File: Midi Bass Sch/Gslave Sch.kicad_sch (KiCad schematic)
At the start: 12 parts, among them SW6 G-slave Reset, U8 PIC16F1789

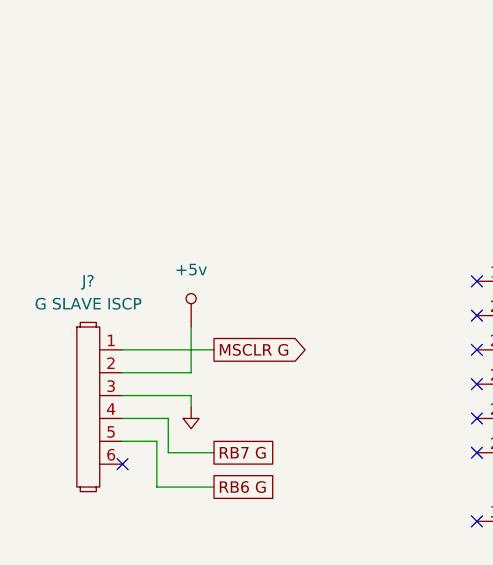
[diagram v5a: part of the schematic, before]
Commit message: started basic pcb layout for Master pic
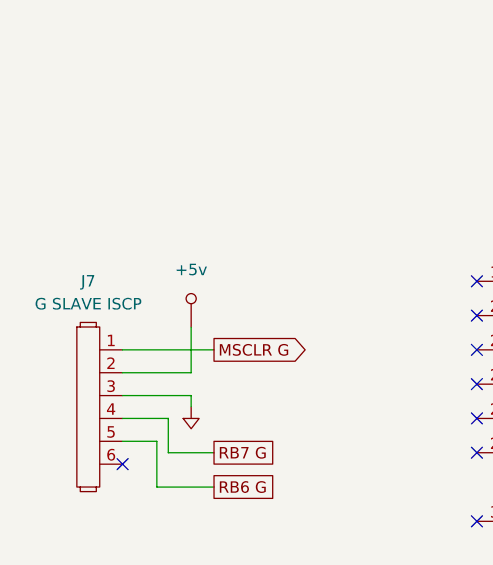
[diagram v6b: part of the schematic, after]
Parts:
- gave numbers to parts that had none: 1
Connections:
- net MSCLR G: now also D20.1; no longer D20.2
- net at C6.1, R55.1, SW6.2: now also D20.2; no longer D20.1
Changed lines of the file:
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@@
 		(dnp no)
 		(fields_autoplaced yes)
-		(property "Reference" "J?"
+		(property "Reference" "J7"
 			(at 25.4 46.99 0)
 			(effects
@@
 			(project "Midi Bass Sch"
 				(path "/06818073-fb22-48ee-acc5-6dedd827034e/a79027be-e76c-43a0-a80a-a6c6a159c340"
-					(reference "J?")
+					(reference "J7")
 					(unit 1)
 				)
@@
 		(dnp no)
 		(fields_autoplaced yes)
-		(property "Reference" "#PWR084"
+		(property "Reference" "#PWR088"
 			(at 175.26 125.73 0)
 			(effects
@@
 			(project "Midi Bass Sch"
 				(path "/06818073-fb22-48ee-acc5-6dedd827034e/a79027be-e76c-43a0-a80a-a6c6a159c340"
-					(reference "#PWR084")
+					(reference "#PWR088")
 					(unit 1)
 				)
@@
 		(dnp no)
 		(fields_autoplaced yes)
-		(property "Reference" "#PWR081"
+		(property "Reference" "#PWR085"
 			(at 46.99 138.43 0)
 			(effects
@@
 			(project "Midi Bass Sch"
 				(path "/06818073-fb22-48ee-acc5-6dedd827034e/a79027be-e76c-43a0-a80a-a6c6a159c340"
-					(reference "#PWR081")
+					(reference "#PWR085")
 					(unit 1)
 				)
@@
 		(dnp no)
 		(fields_autoplaced yes)
-		(property "Reference" "#PWR083"
+		(property "Reference" "#PWR087"
 			(at 108.8644 20.4216 0)
 			(effects
@@
 			(project "Midi Bass Sch"
 				(path "/06818073-fb22-48ee-acc5-6dedd827034e/a79027be-e76c-43a0-a80a-a6c6a159c340"
-					(reference "#PWR083")
+					(reference "#PWR087")
 					(unit 1)
 				)
@@
 		(dnp no)
 		(fields_autoplaced yes)
-		(property "Reference" "#PWR080"
+		(property "Reference" "#PWR084"
 			(at 51.7144 116.9416 0)
 			(effects
@@
 			(project "Midi Bass Sch"
 				(path "/06818073-fb22-48ee-acc5-6dedd827034e/a79027be-e76c-43a0-a80a-a6c6a159c340"
-					(reference "#PWR080")
+					(reference "#PWR084")
 					(unit 1)
 				)
@@
 		(dnp no)
 		(fields_autoplaced yes)
-		(property "Reference" "#PWR082"
+		(property "Reference" "#PWR086"
 			(at 101.6 157.48 0)
 			(effects
@@
 			(project "Midi Bass Sch"
 				(path "/06818073-fb22-48ee-acc5-6dedd827034e/a79027be-e76c-43a0-a80a-a6c6a159c340"
-					(reference "#PWR082")
+					(reference "#PWR086")
 					(unit 1)
 				)
@@
 		(dnp no)
 		(fields_autoplaced yes)
-		(property "Reference" "#PWR0326"
+		(property "Reference" "#PWR082"
 			(at 41.5544 47.0916 0)
 			(effects
@@
 			(project "Midi Bass Sch"
 				(path "/06818073-fb22-48ee-acc5-6dedd827034e/a79027be-e76c-43a0-a80a-a6c6a159c340"
-					(reference "#PWR0326")
+					(reference "#PWR082")
 					(unit 1)
 				)
@@
 		(dnp no)
 		(fields_autoplaced yes)
-		(property "Reference" "#PWR079"
+		(property "Reference" "#PWR081"
 			(at 25.4 139.7 0)
 			(effects
@@
 			(project "Midi Bass Sch"
 				(path "/06818073-fb22-48ee-acc5-6dedd827034e/a79027be-e76c-43a0-a80a-a6c6a159c340"
-					(reference "#PWR079")
+					(reference "#PWR081")
 					(unit 1)
 				)
@@
 		(dnp no)
 		(fields_autoplaced yes)
-		(property "Reference" "#PWR0327"
+		(property "Reference" "#PWR083"
 			(at 36.83 59.69 0)
 			(effects
@@
 			(project "Midi Bass Sch"
 				(path "/06818073-fb22-48ee-acc5-6dedd827034e/a79027be-e76c-43a0-a80a-a6c6a159c340"
-					(reference "#PWR0327")
+					(reference "#PWR083")
 					(unit 1)
 				)
@@
 		(dnp no)
 		(fields_autoplaced yes)
-		(property "Reference" "#PWR085"
+		(property "Reference" "#PWR089"
 			(at 189.23 123.19 0)
 			(effects
@@
 			(project "Midi Bass Sch"
 				(path "/06818073-fb22-48ee-acc5-6dedd827034e/a79027be-e76c-43a0-a80a-a6c6a159c340"
-					(reference "#PWR085")
-					(unit 1)
-				)
+					(reference "#PWR089")
+					(unit 1)
+				)

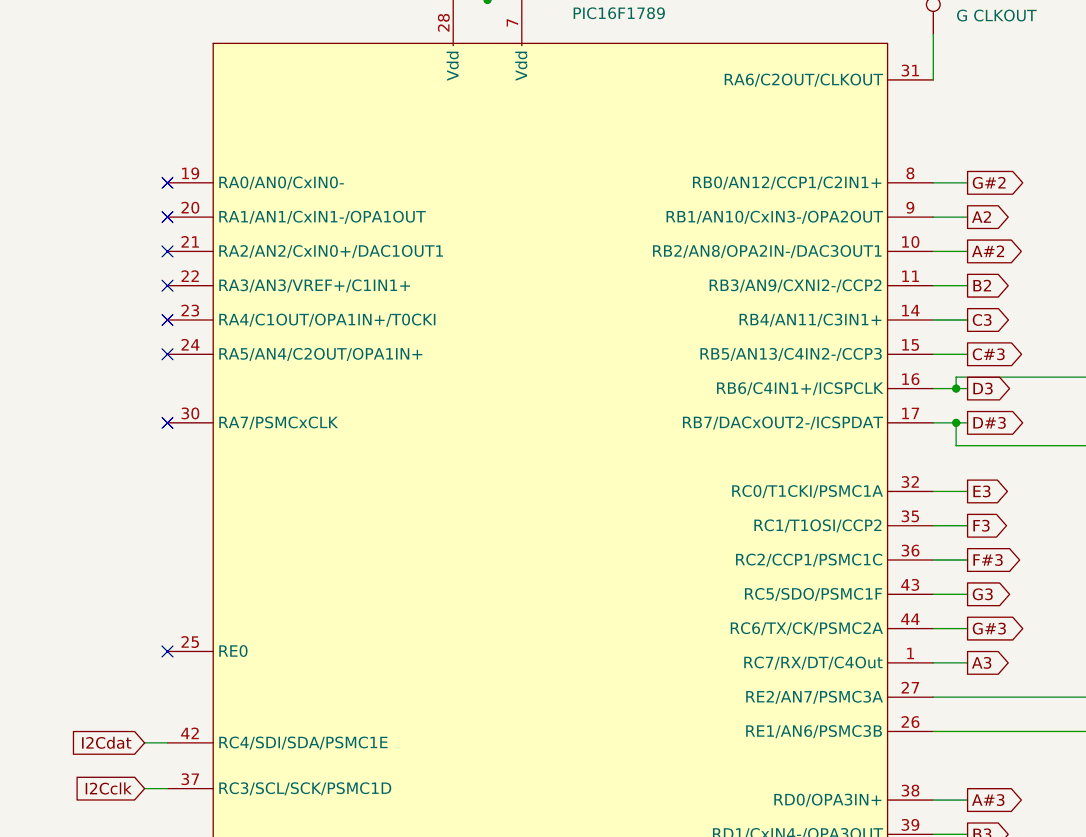
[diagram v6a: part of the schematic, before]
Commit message: updated schematic to reflect code
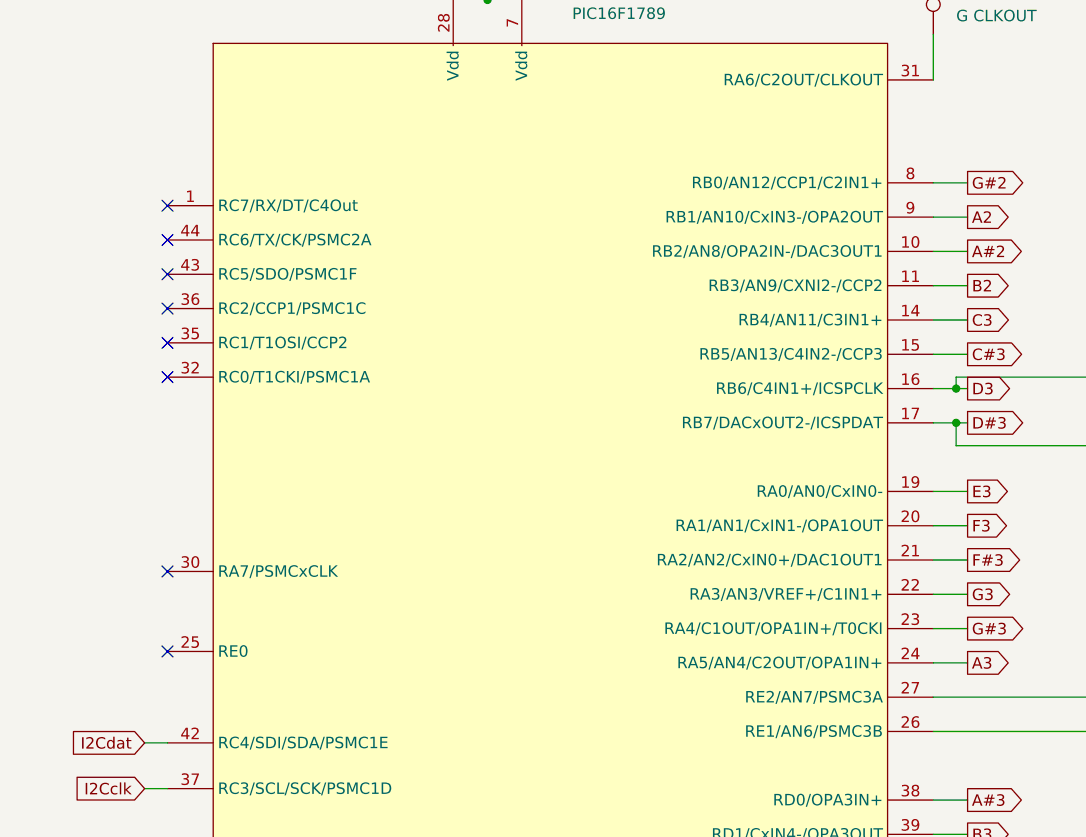
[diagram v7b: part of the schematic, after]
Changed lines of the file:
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@@
 	)
 	(no_connect
-		(at 68.58 66.04)
+		(at 68.58 68.58)
 	)
 	(no_connect
@@
 	)
 	(no_connect
-		(at 68.58 73.66)
+		(at 68.58 90.17)
 	)
 	(no_connect
-		(at 68.58 54.61)
+		(at 68.58 57.15)
 	)
 	(no_connect
@@
 	)
 	(no_connect
-		(at 68.58 62.23)
+		(at 68.58 64.77)
 	)
 	(no_connect
-		(at 68.58 46.99)
+		(at 68.58 49.53)
 	)
 	(no_connect
-		(at 68.58 58.42)
+		(at 68.58 60.96)
 	)
 	(no_connect
-		(at 68.58 50.8)
+		(at 68.58 53.34)
 	)
 	(wire

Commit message: working on troubleshooting section of report
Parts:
- renumbered J7 to J8, R54 to R66, R55 to R67, R56 to R68, R57 to R69, U8 to U10
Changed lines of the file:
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@@
 		(dnp no)
 		(fields_autoplaced yes)
-		(property "Reference" "R56"
+		(property "Reference" "R68"
 			(at 177.8 111.7599 90)
 			(effects
@@
 			(project "Midi Bass Sch"
 				(path "/06818073-fb22-48ee-acc5-6dedd827034e/a79027be-e76c-43a0-a80a-a6c6a159c340"
-					(reference "R56")
+					(reference "R68")
 					(unit 1)
 				)
@@
 		(dnp no)
 		(fields_autoplaced yes)
-		(property "Reference" "R55"
+		(property "Reference" "R67"
 			(at 49.53 124.4599 90)
 			(effects
@@
 			(project "Midi Bass Sch"
 				(path "/06818073-fb22-48ee-acc5-6dedd827034e/a79027be-e76c-43a0-a80a-a6c6a159c340"
-					(reference "R55")
+					(reference "R67")
 					(unit 1)
 				)
@@
 		(dnp no)
 		(fields_autoplaced yes)
-		(property "Reference" "J7"
+		(property "Reference" "J8"
 			(at 25.4 46.99 0)
 			(effects
@@
 			(project "Midi Bass Sch"
 				(path "/06818073-fb22-48ee-acc5-6dedd827034e/a79027be-e76c-43a0-a80a-a6c6a159c340"
-					(reference "J7")
+					(reference "J8")
 					(unit 1)
 				)
@@
 		(dnp no)
 		(fields_autoplaced yes)
-		(property "Reference" "R57"
+		(property "Reference" "R69"
 			(at 191.77 109.2199 90)
 			(effects
@@
 			(project "Midi Bass Sch"
 				(path "/06818073-fb22-48ee-acc5-6dedd827034e/a79027be-e76c-43a0-a80a-a6c6a159c340"
-					(reference "R57")
+					(reference "R69")
 					(unit 1)
 				)
@@
 		(on_board yes)
 		(dnp no)
-		(property "Reference" "U8"
+		(property "Reference" "U10"
 			(at 113.538 25.4 0)
 			(effects
@@
 			(project "Midi Bass Sch"
 				(path "/06818073-fb22-48ee-acc5-6dedd827034e/a79027be-e76c-43a0-a80a-a6c6a159c340"
-					(reference "U8")
+					(reference "U10")
 					(unit 1)
 				)
@@
 		(dnp no)
 		(fields_autoplaced yes)
-		(property "Reference" "#PWR088"
+		(property "Reference" "#PWR0102"
 			(at 175.26 125.73 0)
 			(effects
@@
 			(project "Midi Bass Sch"
 				(path "/06818073-fb22-48ee-acc5-6dedd827034e/a79027be-e76c-43a0-a80a-a6c6a159c340"
-					(reference "#PWR088")
+					(reference "#PWR0102")
 					(unit 1)
 				)
@@
 		(dnp no)
 		(fields_autoplaced yes)
-		(property "Reference" "#PWR085"
+		(property "Reference" "#PWR099"
 			(at 46.99 138.43 0)
 			(effects
@@
 			(project "Midi Bass Sch"
 				(path "/06818073-fb22-48ee-acc5-6dedd827034e/a79027be-e76c-43a0-a80a-a6c6a159c340"
-					(reference "#PWR085")
+					(reference "#PWR099")
 					(unit 1)
 				)
@@
 		(dnp no)
 		(fields_autoplaced yes)
-		(property "Reference" "#PWR087"
+		(property "Reference" "#PWR0101"
 			(at 108.8644 20.4216 0)
 			(effects
@@
 			(project "Midi Bass Sch"
 				(path "/06818073-fb22-48ee-acc5-6dedd827034e/a79027be-e76c-43a0-a80a-a6c6a159c340"
-					(reference "#PWR087")
+					(reference "#PWR0101")
 					(unit 1)
 				)
@@
 		(dnp no)
 		(fields_autoplaced yes)
-		(property "Reference" "#PWR084"
+		(property "Reference" "#PWR098"
 			(at 51.7144 116.9416 0)
 			(effects
@@
 			(project "Midi Bass Sch"
 				(path "/06818073-fb22-48ee-acc5-6dedd827034e/a79027be-e76c-43a0-a80a-a6c6a159c340"
-					(reference "#PWR084")
+					(reference "#PWR098")
 					(unit 1)
 				)
@@
 		(dnp no)
 		(fields_autoplaced yes)
-		(property "Reference" "#PWR086"
+		(property "Reference" "#PWR0100"
 			(at 101.6 157.48 0)
 			(effects
@@
 			(project "Midi Bass Sch"
 				(path "/06818073-fb22-48ee-acc5-6dedd827034e/a79027be-e76c-43a0-a80a-a6c6a159c340"
-					(reference "#PWR086")
+					(reference "#PWR0100")
 					(unit 1)
 				)
@@
 		(dnp no)
 		(fields_autoplaced yes)
-		(property "Reference" "#PWR082"
+		(property "Reference" "#PWR096"
 			(at 41.5544 47.0916 0)
 			(effects
@@
 			(project "Midi Bass Sch"
 				(path "/06818073-fb22-48ee-acc5-6dedd827034e/a79027be-e76c-43a0-a80a-a6c6a159c340"
-					(reference "#PWR082")
+					(reference "#PWR096")
 					(unit 1)
 				)
@@
 		(dnp no)
 		(fields_autoplaced yes)
-		(property "Reference" "#PWR081"
+		(property "Reference" "#PWR095"
 			(at 25.4 139.7 0)
 			(effects
@@
 			(project "Midi Bass Sch"
 				(path "/06818073-fb22-48ee-acc5-6dedd827034e/a79027be-e76c-43a0-a80a-a6c6a159c340"
-					(reference "#PWR081")
+					(reference "#PWR095")
 					(unit 1)
 				)
@@
 		(dnp no)
 		(fields_autoplaced yes)
-		(property "Reference" "R54"
+		(property "Reference" "R66"
 			(at 27.94 135.8899 90)
 			(effects
@@
 			(project "Midi Bass Sch"
 				(path "/06818073-fb22-48ee-acc5-6dedd827034e/a79027be-e76c-43a0-a80a-a6c6a159c340"
-					(reference "R54")
+					(reference "R66")
 					(unit 1)
 				)
@@
 		(dnp no)
 		(fields_autoplaced yes)
-		(property "Reference" "#PWR083"
+		(property "Reference" "#PWR097"
 			(at 36.83 59.69 0)
 			(effects
@@
 			(project "Midi Bass Sch"
 				(path "/06818073-fb22-48ee-acc5-6dedd827034e/a79027be-e76c-43a0-a80a-a6c6a159c340"
-					(reference "#PWR083")
+					(reference "#PWR097")
 					(unit 1)
 				)
@@
 		(dnp no)
 		(fields_autoplaced yes)
-		(property "Reference" "#PWR089"
+		(property "Reference" "#PWR0103"
 			(at 189.23 123.19 0)
 			(effects
@@
 			(project "Midi Bass Sch"
 				(path "/06818073-fb22-48ee-acc5-6dedd827034e/a79027be-e76c-43a0-a80a-a6c6a159c340"
-					(reference "#PWR089")
-					(unit 1)
-				)
+					(reference "#PWR0103")
+					(unit 1)
+				)
